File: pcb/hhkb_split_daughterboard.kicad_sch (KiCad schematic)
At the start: 9 parts

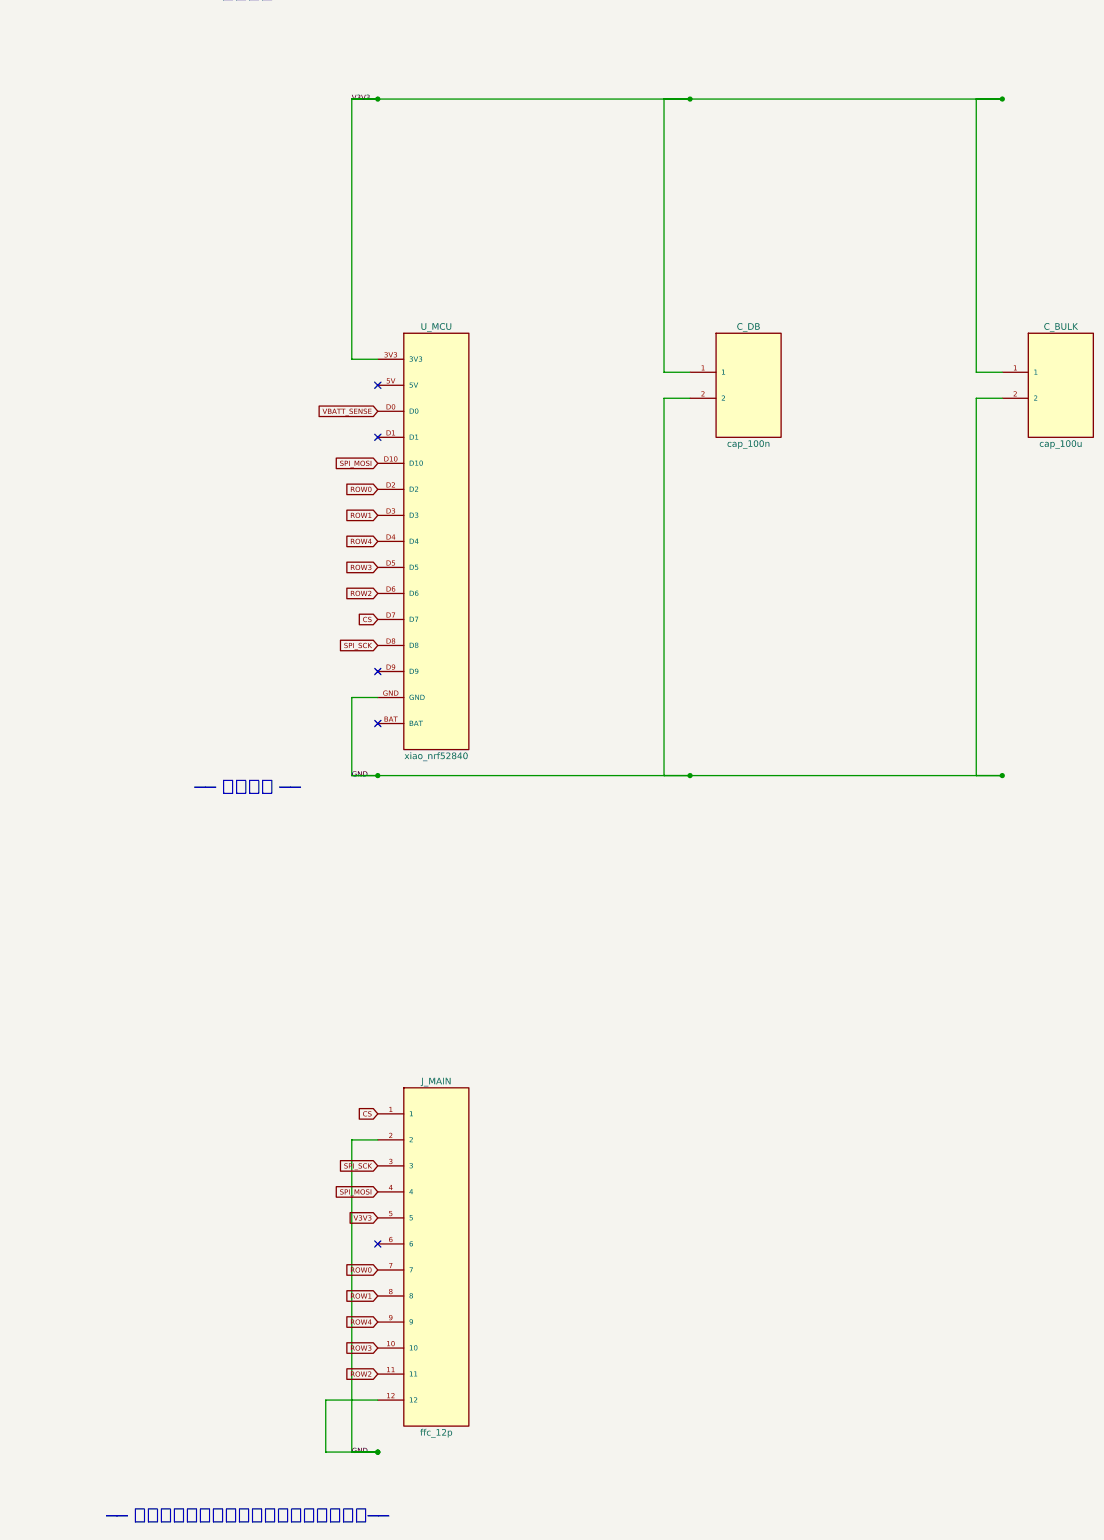
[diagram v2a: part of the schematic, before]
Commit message: C_DB を消した（負荷の直近にいないパスコンだった・#45）
子基板のパスコン C_DB（0.1µF・C49678）を削除した。実装部品が 2 個減る
（左右に 1 個ずつ）。#44 と合わせて、子基板のコンデンサは 0 個になった。

**理由は「相手がいない」ではなく「取り分が誤差」。**3V3 の負荷は最初から
2 つあり、どちらも子基板の外にいた:

  nRF52840 → XIAO の内部。内蔵の 2.2µF ×5 が桁違いに近い
  595 ×2   → 主基板。直近の C_U1/C_U2 が 58:1 で取る

電流は近い順ではなく、ループインダクタンスに反比例して分流する。
足りているところに数 % を足しても改善せず、不足していたなら数 % では
救えない。どちらに転んでも出番が無い。

LDO（SGM2040・型番一致を確認）の安定条件 C_OUT=0.1〜10µF も内部の
公称 11µF が満たす。上限側は既に超えており、外から足す議論は成立しない。

調査文書の結論は独立に再検証してから実行した:

  §1 子基板の 3V3 は 4 パッドで全数  → .kicad_pcb を走査して一致
  §2 XIAO 内部の 2.2µF ×5           → Seeed の KiCad ソース（73 footprint）
                                       を自分で数え直して完全一致
  §3 分流比 58:1                     → 152Ω ÷ 2.6Ω で一致

検査は「C_DB が復活していないこと」ではなく、**その負荷の直近に誰かいるか**
を見る（test_the_daughterboard_has_no_part_that_needs_local_decoupling）。
子基板に 595 を足す／ICS を空にする、の 2 通りで落ちることを確認済み。

ICS から xiao_nrf52840 を外した。XIAO は IC ではなくモジュールで内蔵して
いるため。「XIAO にパスコンが無い」と足し直されないよう理由をコードに残した。

子基板 DRC: 違反 0 / 未配線 0 / 警告 0。回路図は部品 8 → 7 個。

⚠️ 電源部（R_LO/R_HI/SW_PWR/D_PWR）は動かしていない。利用者が KiCad で
釣り合いを取った値で、SILK_REF の余白が 0.15mm ぎりぎりのため。

Co-Authored-By: Claude Opus 5 (1M context) <noreply@anthropic.com>
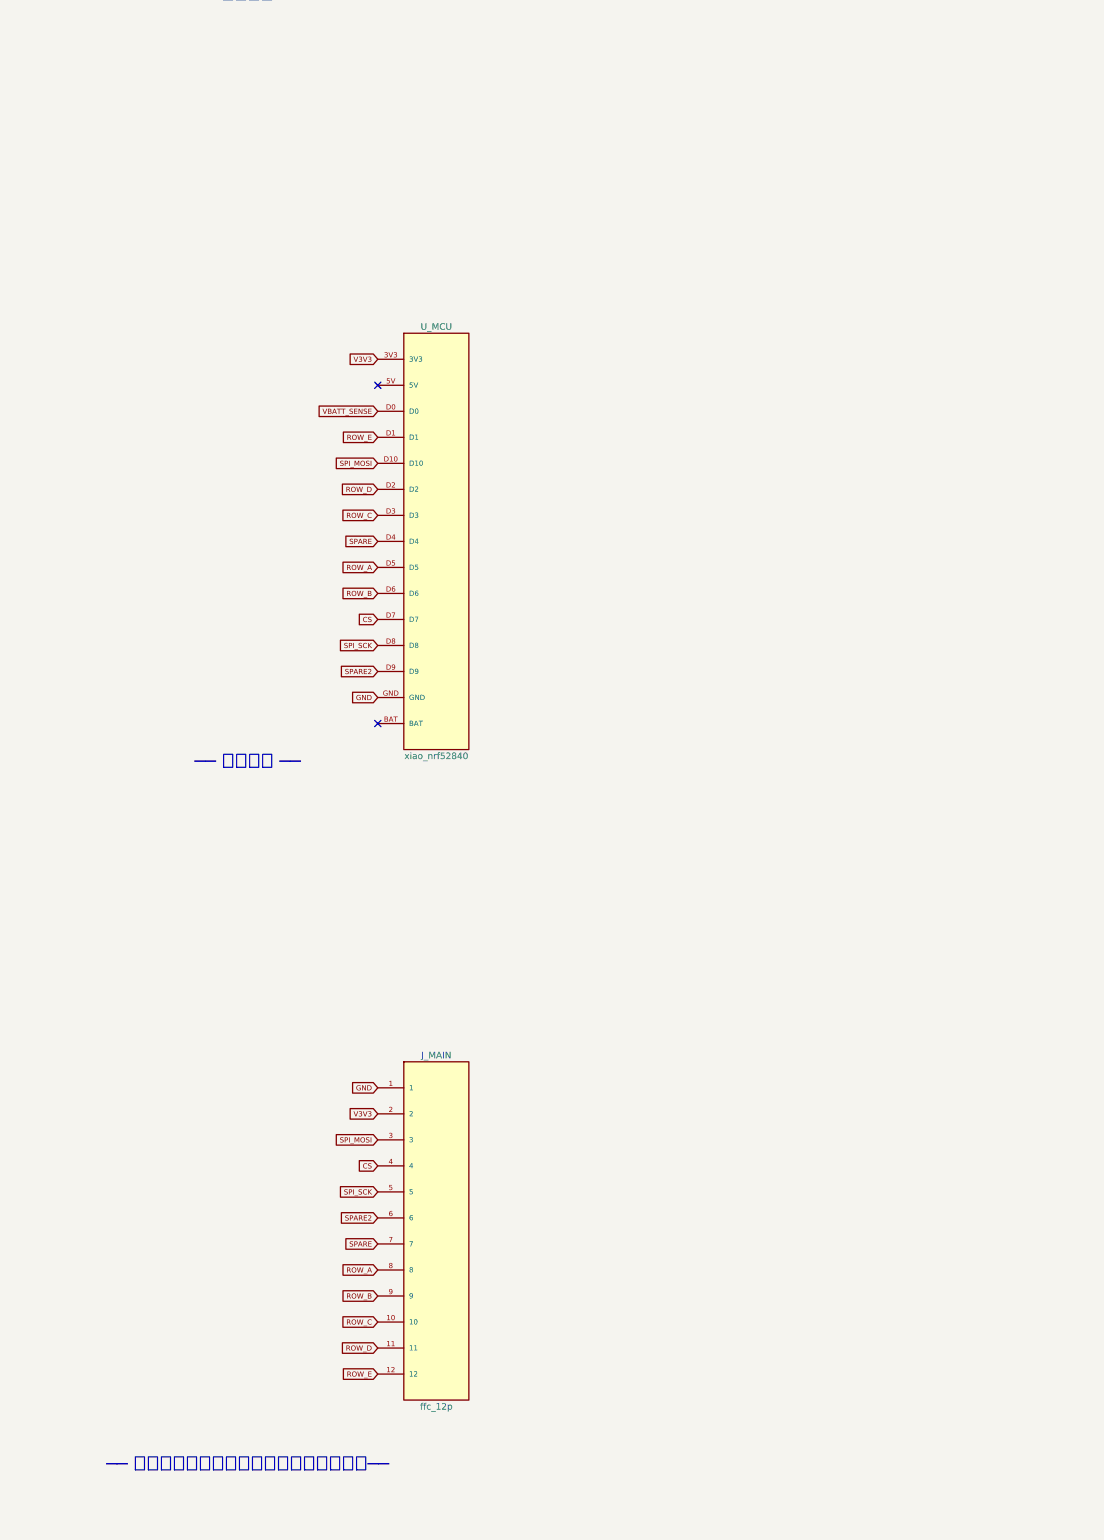
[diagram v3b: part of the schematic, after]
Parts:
- removed C_BULK: cap_100u, symbol hhkb_split_daughterboard:cap_100u
- removed C_DB: cap_100n, symbol hhkb_split_daughterboard:cap_100n
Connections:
- net CS: now also J_MAIN.4; no longer J_MAIN.1
- net GND: now also J_MAIN.1; no longer J_MAIN.12, J_MAIN.2
- net SPI_MOSI: now also J_MAIN.3; no longer J_MAIN.4
- net SPI_SCK: now also J_MAIN.5; no longer J_MAIN.3
- net V3V3: now also J_MAIN.2; no longer J_MAIN.5
- net ROW_E: now reaches U_MCU.D1
- net ROW_E: now also J_MAIN.12
- net SPARE2: now reaches U_MCU.D9
- net SPARE2: now also J_MAIN.6
- net ROW0 renamed ROW_D
- net ROW_D: now also J_MAIN.11; no longer J_MAIN.7
- net ROW1 renamed ROW_A
- net ROW_A: now also U_MCU.D5; no longer U_MCU.D3
- net ROW2 renamed ROW_B
- net ROW_B: now also J_MAIN.9; no longer J_MAIN.11
- net ROW3 renamed ROW_C
- net ROW_C: now also U_MCU.D3; no longer U_MCU.D5
- net ROW4 renamed SPARE
- net SPARE: now also J_MAIN.7; no longer J_MAIN.9
- no-connect marks 5 -> 2
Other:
- moved on the sheet: J_MAIN
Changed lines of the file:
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@@
 	(generator "hhkb_split")
 	(generator_version "10.0")
-	(paper "User" 295.91 480.06)
+	(paper "User" 295.91 469.90)
 	(title_block
 		(title "hhkb_split_daughterboard")
@@
 		(effects (font (size 1.0 1.0)))
 	)
+	(global_label
+		"V3V3"
+		(shape input)
+		(at 63.50 190.50 180)
+		(effects (font (size 1.0 1.0)))
+	)
 	(no_connect (at 63.50 195.58))
 	(global_label
@@
 		(effects (font (size 1.0 1.0)))
 	)
-	(no_connect (at 63.50 205.74))
+	(global_label
+		"ROW_E"
+		(shape input)
+		(at 63.50 205.74 180)
+		(effects (font (size 1.0 1.0)))
+	)
 	(global_label
 		"SPI_MOSI"
@@
 	)
 	(global_label
-		"ROW0"
+		"ROW_D"
 		(shape input)
 		(at 63.50 215.90 180)
@@
 	)
 	(global_label
-		"ROW1"
+		"ROW_C"
 		(shape input)
 		(at 63.50 220.98 180)
@@
 	)
 	(global_label
-		"ROW4"
+		"SPARE"
 		(shape input)
 		(at 63.50 226.06 180)
@@
 	)
 	(global_label
-		"ROW3"
+		"ROW_A"
 		(shape input)
 		(at 63.50 231.14 180)
@@
 	)
 	(global_label
-		"ROW2"
+		"ROW_B"
 		(shape input)
 		(at 63.50 236.22 180)
@@
 		(effects (font (size 1.0 1.0)))
 	)
-	(no_connect (at 63.50 251.46))
+	(global_label
+		"SPARE2"
+		(shape input)
+		(at 63.50 251.46 180)
+		(effects (font (size 1.0 1.0)))
+	)
+	(global_label
+		"GND"
+		(shape input)
+		(at 63.50 256.54 180)
+		(effects (font (size 1.0 1.0)))
+	)
 	(no_connect (at 63.50 261.62))
 	(global_label
+		"GND"
+		(shape input)
+		(at 63.50 332.74 180)
+		(effects (font (size 1.0 1.0)))
+	)
+	(global_label
+		"V3V3"
+		(shape input)
+		(at 63.50 337.82 180)
+		(effects (font (size 1.0 1.0)))
+	)
+	(global_label
+		"SPI_MOSI"
+		(shape input)
+		(at 63.50 342.90 180)
+		(effects (font (size 1.0 1.0)))
+	)
+	(global_label
 		"CS"
 		(shape input)
-		(at 63.50 337.82 180)
+		(at 63.50 347.98 180)
 		(effects (font (size 1.0 1.0)))
 	)
@@
 		"SPI_SCK"
 		(shape input)
-		(at 63.50 347.98 180)
-		(effects (font (size 1.0 1.0)))
-	)
-	(global_label
-		"SPI_MOSI"
-		(shape input)
 		(at 63.50 353.06 180)
 		(effects (font (size 1.0 1.0)))
 	)
 	(global_label
-		"V3V3"
+		"SPARE2"
 		(shape input)
 		(at 63.50 358.14 180)
 		(effects (font (size 1.0 1.0)))
 	)
-	(no_connect (at 63.50 363.22))
-	(global_label
-		"ROW0"
+	(global_label
+		"SPARE"
+		(shape input)
+		(at 63.50 363.22 180)
+		(effects (font (size 1.0 1.0)))
+	)
+	(global_label
+		"ROW_A"
 		(shape input)
 		(at 63.50 368.30 180)
@@
 	)
 	(global_label
-		"ROW1"
+		"ROW_B"
 		(shape input)
 		(at 63.50 373.38 180)
@@
 	)
 	(global_label
-		"ROW4"
+		"ROW_C"
 		(shape input)
 		(at 63.50 378.46 180)
@@
 	)
 	(global_label
-		"ROW3"
+		"ROW_D"
 		(shape input)
 		(at 63.50 383.54 180)
@@
 	)
 	(global_label
-		"ROW2"
+		"ROW_E"
 		(shape input)
 		(at 63.50 388.62 180)
@@
 	)
 	(wire
-		(pts (xy 58.42 139.70) (xy 185.42 139.70))
-		(stroke (width 0.508) (type default))
-	)
-	(label
-		"V3V3"
-		(at 58.42 139.70 0)
-		(effects (font (size 1.0 1.0)))
-	)
-	(wire
-		(pts (xy 58.42 271.78) (xy 185.42 271.78))
-		(stroke (width 0.508) (type default))
-	)
-	(label
-		"GND"
-		(at 58.42 271.78 0)
-		(effects (font (size 1.0 1.0)))
-	)
-	(wire
-		(pts (xy 58.42 403.86) (xy 63.50 403.86))
-		(stroke (width 0.508) (type default))
-	)
-	(label
-		"GND"
-		(at 58.42 403.86 0)
-		(effects (font (size 1.0 1.0)))
-	)
-	(wire
 		(pts (xy 124.46 68.58) (xy 119.38 68.58))
 		(stroke (width 0) (type default))
@@
 	)
 	(junction (at 124.46 116.84) (diameter 1.016) (color 0 0 0 0)
-	)
-	(wire
-		(pts (xy 63.50 190.50) (xy 58.42 190.50))
-		(stroke (width 0) (type default))
-	)
-	(wire
-		(pts (xy 58.42 190.50) (xy 58.42 139.70))
-		(stroke (width 0) (type default))
-	)
-	(wire
-		(pts (xy 58.42 139.70) (xy 63.50 139.70))
-		(stroke (width 0) (type default))
-	)
-	(junction (at 63.50 139.70) (diameter 1.016) (color 0 0 0 0)
-	)
-	(wire
-		(pts (xy 124.46 193.04) (xy 119.38 193.04))
-		(stroke (width 0) (type default))
-	)
-	(wire
-		(pts (xy 119.38 193.04) (xy 119.38 139.70))
-		(stroke (width 0) (type default))
-	)
-	(wire
-		(pts (xy 119.38 139.70) (xy 124.46 139.70))
-		(stroke (width 0) (type default))
-	)
-	(junction (at 124.46 139.70) (diameter 1.016) (color 0 0 0 0)
-	)
-	(wire
-		(pts (xy 185.42 193.04) (xy 180.34 193.04))
-		(stroke (width 0) (type default))
-	)
-	(wire
-		(pts (xy 180.34 193.04) (xy 180.34 139.70))
-		(stroke (width 0) (type default))
-	)
-	(wire
-		(pts (xy 180.34 139.70) (xy 185.42 139.70))
-		(stroke (width 0) (type default))
-	)
-	(junction (at 185.42 139.70) (diameter 1.016) (color 0 0 0 0)
-	)
-	(wire
-		(pts (xy 63.50 256.54) (xy 58.42 256.54))
-		(stroke (width 0) (type default))
-	)
-	(wire
-		(pts (xy 58.42 256.54) (xy 58.42 271.78))
-		(stroke (width 0) (type default))
-	)
-	(wire
-		(pts (xy 58.42 271.78) (xy 63.50 271.78))
-		(stroke (width 0) (type default))
-	)
-	(junction (at 63.50 271.78) (diameter 1.016) (color 0 0 0 0)
-	)
-	(wire
-		(pts (xy 124.46 198.12) (xy 119.38 198.12))
-		(stroke (width 0) (type default))
-	)
-	(wire
-		(pts (xy 119.38 198.12) (xy 119.38 271.78))
-		(stroke (width 0) (type default))
-	)
-	(wire
-		(pts (xy 119.38 271.78) (xy 124.46 271.78))
-		(stroke (width 0) (type default))
-	)
-	(junction (at 124.46 271.78) (diameter 1.016) (color 0 0 0 0)
-	)
-	(wire
-		(pts (xy 185.42 198.12) (xy 180.34 198.12))
-		(stroke (width 0) (type default))
-	)
-	(wire
-		(pts (xy 180.34 198.12) (xy 180.34 271.78))
-		(stroke (width 0) (type default))
-	)
-	(wire
-		(pts (xy 180.34 271.78) (xy 185.42 271.78))
-		(stroke (width 0) (type default))
-	)
-	(junction (at 185.42 271.78) (diameter 1.016) (color 0 0 0 0)
-	)
-	(wire
-		(pts (xy 63.50 342.90) (xy 58.42 342.90))
-		(stroke (width 0) (type default))
-	)
-	(wire
-		(pts (xy 58.42 342.90) (xy 58.42 403.86))
-		(stroke (width 0) (type default))
-	)
-	(wire
-		(pts (xy 58.42 403.86) (xy 63.50 403.86))
-		(stroke (width 0) (type default))
-	)
-	(junction (at 63.50 403.86) (diameter 1.016) (color 0 0 0 0)
-	)
-	(wire
-		(pts (xy 63.50 393.70) (xy 53.34 393.70))
-		(stroke (width 0) (type default))
-	)
-	(wire
-		(pts (xy 53.34 393.70) (xy 53.34 403.86))
-		(stroke (width 0) (type default))
-	)
-	(wire
-		(pts (xy 53.34 403.86) (xy 63.50 403.86))
-		(stroke (width 0) (type default))
-	)
-	(junction (at 63.50 403.86) (diameter 1.016) (color 0 0 0 0)
 	)
 	(text "── 電源 ──"
@@
 	)
 	(text "── ケーブル ──"
-		(at 38.10 274.32 0)
+		(at 38.10 269.24 0)
 		(effects (font (size 2.54 2.54)))
 	)
 	(text "── 電源フラグ（基板の外から来るネット）──"
-		(at 38.10 416.56 0)
+		(at 38.10 406.40 0)
 		(effects (font (size 2.54 2.54)))
 	)
@@
 	)
 	(symbol
-		(lib_id "hhkb_split_daughterboard:cap_100n")
-		(at 135.89 195.58 0)
-		(unit 1)
-		(exclude_from_sim no)
-		(in_bom yes)
-		(on_board yes)
-		(dnp no)
-		(property "Reference" "C_DB" (at 135.89 184.15 0) (effects (font (size 1.27 1.27))))
-		(property "Value" "cap_100n" (at 135.89 207.01 0) (effects (font (size 1.27 1.27))))
+		(lib_id "hhkb_split_daughterboard:ffc_12p")
+		(at 74.93 360.68 0)
+		(unit 1)
+		(exclude_from_sim no)
+		(in_bom yes)
+		(on_board yes)
+		(dnp no)
+		(property "Reference" "J_MAIN" (at 74.93 326.39 0) (effects (font (size 1.27 1.27))))
+		(property "Value" "ffc_12p" (at 74.93 394.97 0) (effects (font (size 1.27 1.27))))
 		(pin "1")
 		(pin "2")
-		(instances
-			(project "hhkb_split_daughterboard"
-				(path "/569e6ce2-5cbf-5b99-8a67-ce450b40985c"
-					(reference "C_DB")
-					(unit 1)
-				)
-			)
-		)
-	)
-	(symbol
-		(lib_id "hhkb_split_daughterboard:cap_100u")
-		(at 196.85 195.58 0)
-		(unit 1)
-		(exclude_from_sim no)
-		(in_bom yes)
-		(on_board yes)
-		(dnp no)
-		(property "Reference" "C_BULK" (at 196.85 184.15 0) (effects (font (size 1.27 1.27))))
-		(property "Value" "cap_100u" (at 196.85 207.01 0) (effects (font (size 1.27 1.27))))
-		(pin "1")
-		(pin "2")
-		(instances
-			(project "hhkb_split_daughterboard"
-				(path "/569e6ce2-5cbf-5b99-8a67-ce450b40985c"
-					(reference "C_BULK")
-					(unit 1)
-				)
-			)
-		)
-	)
-	(symbol
-		(lib_id "hhkb_split_daughterboard:ffc_12p")
-		(at 74.93 365.76 0)
-		(unit 1)
-		(exclude_from_sim no)
-		(in_bom yes)
-		(on_board yes)
-		(dnp no)
-		(property "Reference" "J_MAIN" (at 74.93 331.47 0) (effects (font (size 1.27 1.27))))
-		(property "Value" "ffc_12p" (at 74.93 400.05 0) (effects (font (size 1.27 1.27))))
-		(pin "1")
-		(pin "2")
